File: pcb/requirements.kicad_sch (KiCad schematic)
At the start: 2 parts

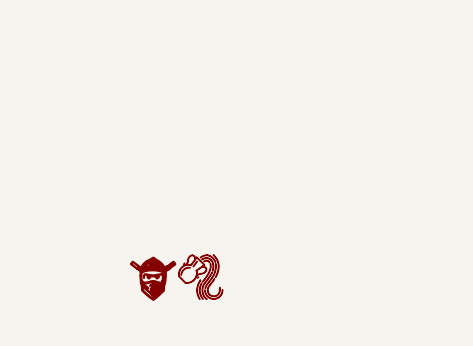
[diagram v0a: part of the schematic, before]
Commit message: added open hw; changed test points; added pulls on buttons
change buttons to be 2 connectors with pull ups.
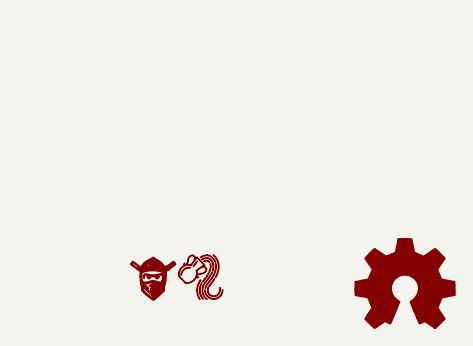
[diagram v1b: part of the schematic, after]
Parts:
- added LOGO3: Logo_Open_Hardware_Small, Symbol:OSHW-Logo_5.7x6mm_SilkScreen, symbol Graphic:Logo_Open_Hardware_Small
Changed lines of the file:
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@@
+	)
+	(symbol
+		(lib_id "Graphic:Logo_Open_Hardware_Small")
+		(at 212.09 172.72 0)
+		(unit 1)
+		(exclude_from_sim no)
+		(in_bom no)
+		(on_board yes)
+		(dnp no)
+		(property "Reference" "LOGO3"
+			(at 212.09 165.735 0)
+			(effects
+				(font
+					(size 1.27 1.27)
+				)
+				(hide yes)
+			)
+		)
+		(property "Value" "Logo_Open_Hardware_Small"
+			(at 212.09 178.435 0)
+			(effects
+				(font
+					(size 1.27 1.27)
+				)
+				(hide yes)
+			)
+		)
+		(property "Footprint" "Symbol:OSHW-Logo_5.7x6mm_SilkScreen"
+			(at 212.09 172.72 0)
+			(effects
+				(font
+					(size 1.27 1.27)
+				)
+				(hide yes)
+			)
+		)
+		(property "Datasheet" "~"
+			(at 212.09 172.72 0)
+			(effects
+				(font
+					(size 1.27 1.27)
+				)
+				(hide yes)
+			)
+		)
+		(property "Description" "Open Hardware logo, small"
+			(at 212.09 172.72 0)
+			(effects
+				(font
+					(size 1.27 1.27)
+				)
+				(hide yes)
+			)
+		)
+		(property "Sim.Enable" "0"
+			(at 212.09 172.72 0)
+			(effects
+				(font
+					(size 1.27 1.27)
+				)
+				(hide yes)
+			)
+		)
+		(instances
+			(project ""
+				(path "/39407804-2746-45a9-a901-1039a9921518/2e166321-b713-45e0-87cf-342f1811c390"
+					(reference "LOGO3")
+					(unit 1)
+				)
+			)
+		)
 	)
 	(symbol

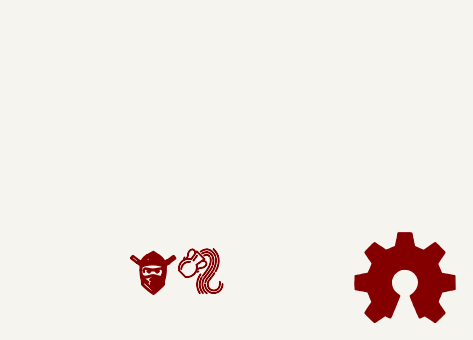
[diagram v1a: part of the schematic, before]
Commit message: Change panel to be 1x1
Changed connectors be vertical rather than horizontal.
Updated TVS diodes to DFN1006 rather than SMF
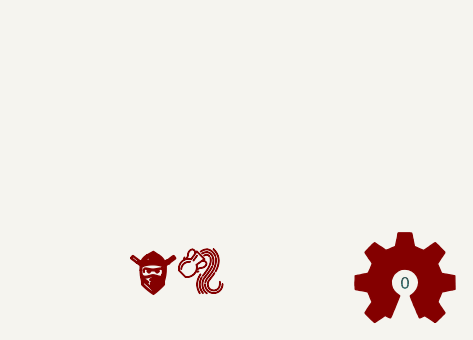
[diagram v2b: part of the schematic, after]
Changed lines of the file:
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@@
 		(at 212.09 172.72 0)
 		(unit 1)
-		(exclude_from_sim no)
+		(exclude_from_sim yes)
 		(in_bom no)
 		(on_board yes)
@@
 					(size 1.27 1.27)
 				)
-				(hide yes)
 			)
 		)

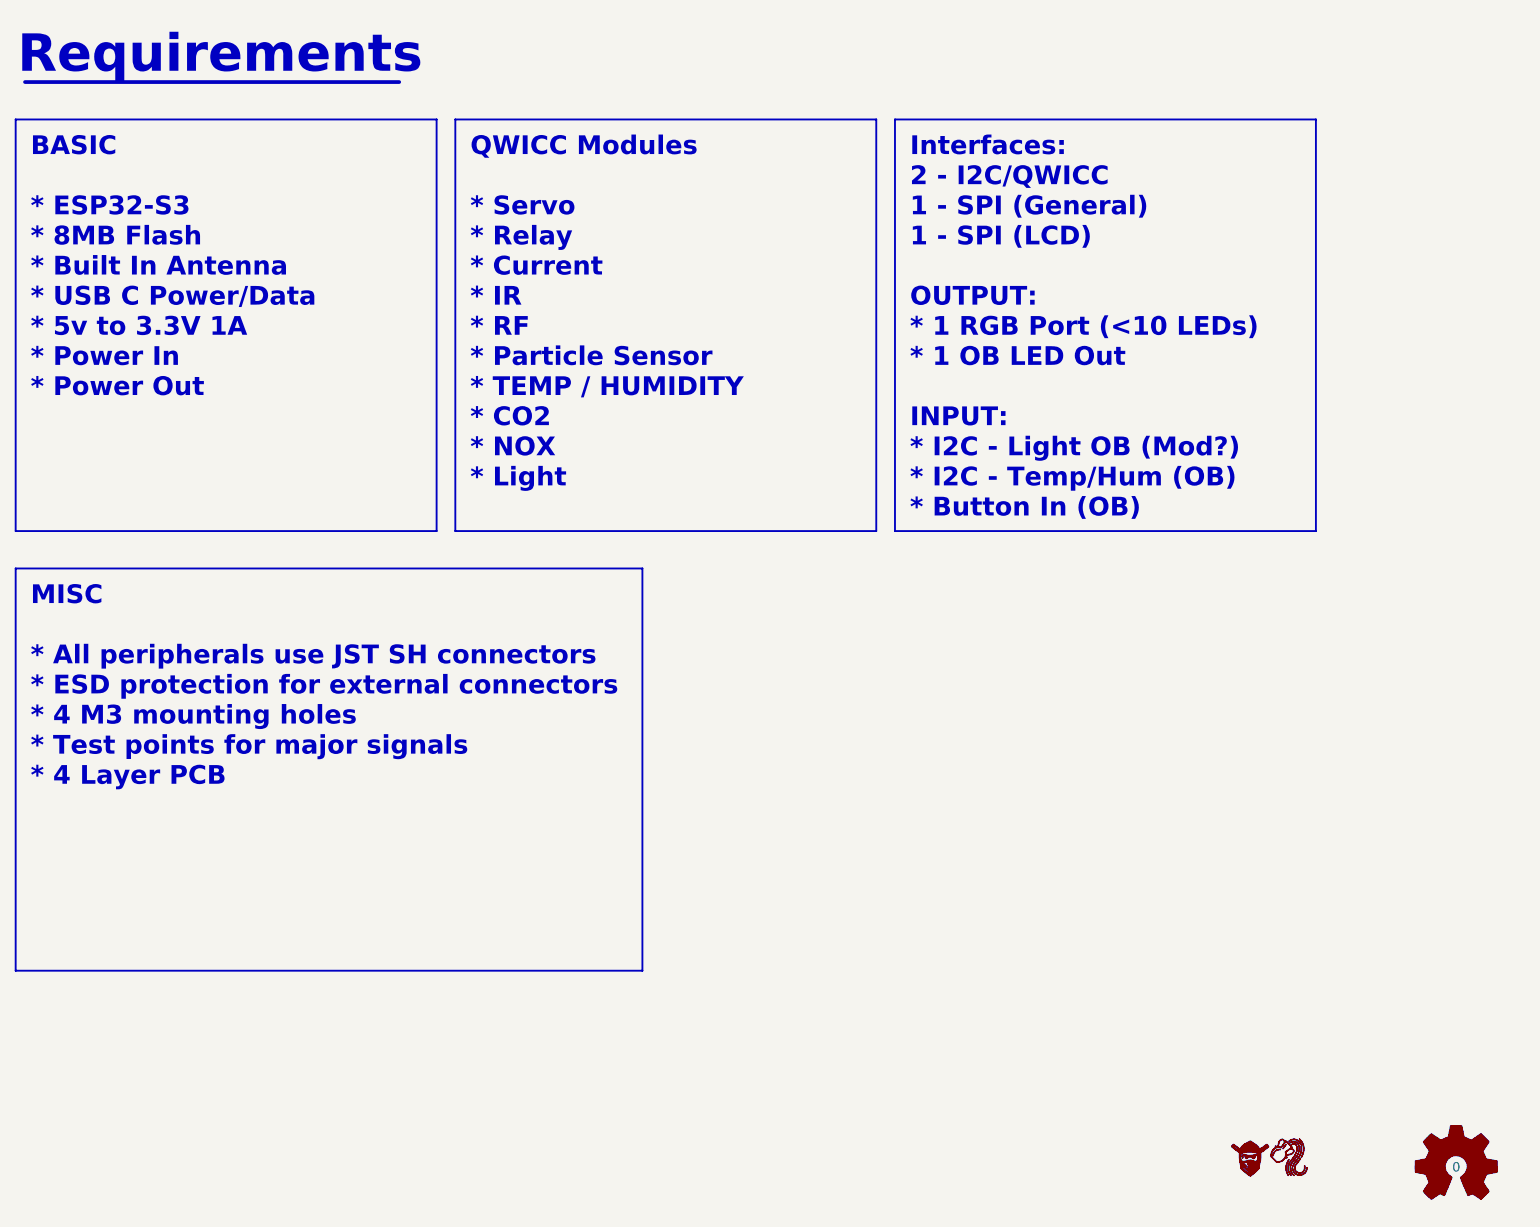
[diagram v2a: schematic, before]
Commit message: Major overhaul of IO
Added GPIO module
Added SPI interface
Added serial interface
Added power selection
Added power LEDs
Changed v3.3 LDO
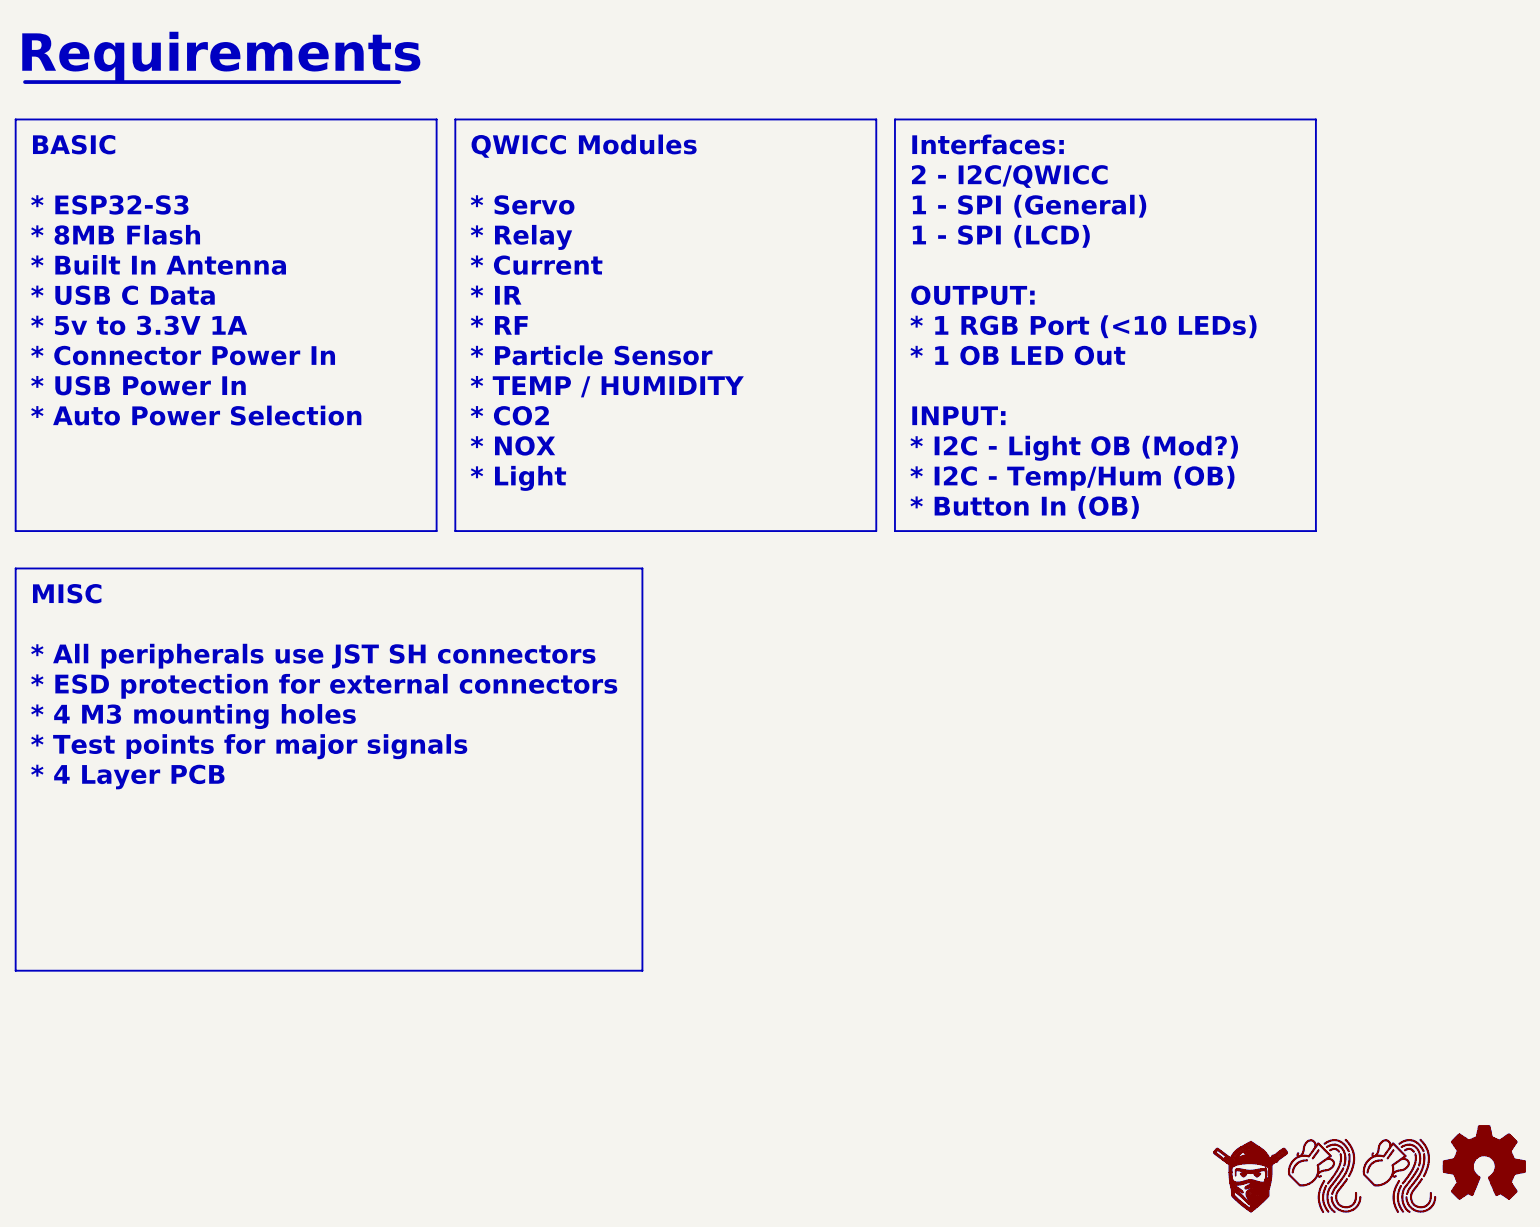
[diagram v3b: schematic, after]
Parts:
- added LOGO4: ~, CRGM Logos:Aquarius Logo 5mm, symbol CRGM Logos:Aquarius Logo

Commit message: Rationalized attributes; excluded some footprints from BOM
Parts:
- LOGO1, LOGO2, LOGO4: now left out of the parts list
- LOGO3: value Logo_Open_Hardware_Small -> ~
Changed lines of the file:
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@@
 			)
 		)
-		(property "Value" "Logo_Open_Hardware_Small"
+		(property "Value" "~"
 			(at 215.9 178.435 0)
 			(effects
@@
 		(unit 1)
 		(exclude_from_sim no)
-		(in_bom yes)
+		(in_bom no)
 		(on_board yes)
 		(dnp no)
@@
 		(unit 1)
 		(exclude_from_sim no)
-		(in_bom yes)
+		(in_bom no)
 		(on_board yes)
 		(dnp no)
@@
 		(unit 1)
 		(exclude_from_sim no)
-		(in_bom yes)
+		(in_bom no)
 		(on_board yes)
 		(dnp no)
